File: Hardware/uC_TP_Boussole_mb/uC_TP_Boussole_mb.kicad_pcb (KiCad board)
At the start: 2 copper layers, 90 x 90 mm, 53 parts, among them J201 Conn_01x04, J301 Conn_01x05, J302 Conn_01x06, J401 Conn_01x02, J701 Conn_01x09, J801 Conn_01x04, SW301 SW_Push, SW302 SW_Push, SW303 SW_Push_DPDT, U201 TMC2225-SA-T, U301 STM32C011J4Mx, U402 AMS1117-3.3, U501 NUCLEO_L476RG

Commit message: update ppcb
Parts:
- added C601: 100n, Capacitor_SMD:C_0402_1005Metric, F.Cu at (70.4, 93.3)
- added U601: ~, Package_TO_SOT_SMD:SOT-363_SC-70-6, F.Cu at (71.0, 90.3)
- R601: value R_Small -> 30m
- moved C901 200.5 mm to (35.0, 89.1)
- moved C902 200.5 mm to (35.0, 91.1)
- moved C903 200.5 mm to (35.0, 93.0)
- moved C904 200.5 mm to (35.0, 95.0)
- moved R901 200.5 mm to (32.1, 89.1)
- moved R902 200.5 mm to (32.1, 91.1)
- moved R903 200.5 mm to (32.1, 93.1)
- moved R904 200.5 mm to (32.1, 95.1)
- moved R905 200.5 mm to (32.1, 97.1)
- moved R906 200.5 mm to (32.1, 99.0)
- moved J701 199.3 mm to (34.5, 112.0), turned to -90 degrees
- moved C801 197.9 mm to (32.5, 65.0)
- moved J801 197.9 mm to (28.8, 66.3)
- moved C701 188.6 mm to (43.5, 123.0)
- moved D401 188.2 mm to (76.8, 66.8)
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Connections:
- C402 pad 1: /Current_NCS199A3RSQT2G/Supply -> +3.3V
- C903 pad 1: /Rotary_Encodeur/ENC_BTN -> /NUCLEO_L476RG/ENC_BTN
- R403 pad 1: /Current_NCS199A3RSQT2G/Supply -> +3.3V
- R601 pad 1: /Current_NCS199A3RSQT2G/Supply -> +5V
- R601 pad 2: +3.3V -> /Current_NCS199A3RSQT2G/Load
- R906 pad 2: /Rotary_Encodeur/ENC_BTN -> /NUCLEO_L476RG/ENC_BTN
- U201 pad 20: /TMC2225_Driver/DIR -> /NUCLEO_L476RG/STEPPER_DIR
- U201 pad 21: /TMC2225_Driver/ENN -> /NUCLEO_L476RG/STEPPER_ENN
- U201 pad 25: /TMC2225_Driver/MS1 -> /NUCLEO_L476RG/STEPPER_MS1
- U201 pad 26: /TMC2225_Driver/MS2 -> /NUCLEO_L476RG/STEPPER_MS2
- U402 pad 2: /Current_NCS199A3RSQT2G/Supply -> +3.3V
- U501 pad 105: +3.3V -> unconnected-(U501A-VDD-Pad105)
- U501 pad 106: +5V -> /Current_NCS199A3RSQT2G/Load
- U501 pad 117: unconnected-(U501B-PA15-Pad117) -> /NUCLEO_L476RG/ENC_BTN
- U501 pad 132: unconnected-(U501B-PA4-Pad132) -> /Current_NCS199A3RSQT2G/Imes
- U501 pad 134: unconnected-(U501B-PB0-Pad134) -> /Magnetometre_BMM150_SEN0419/INT
- U501 pad 136: unconnected-(U501B-PC1-Pad136) -> /Magnetometre_BMM150_SEN0419/STATUS
- U501 pad 138: unconnected-(U501B-PC0-Pad138) -> /Magnetometre_BMM150_SEN0419/SPI_CS
- U501 pad 207: +3.3VA -> unconnected-(U501A-AVDD-Pad207)
- U501 pad 213: unconnected-(U501B-PA6-Pad213) -> /NUCLEO_L476RG/STEPPER_DIR
- U501 pad 214: unconnected-(U501B-PA11-Pad214) -> /NUCLEO_L476RG/STEPPER_MS1
- U501 pad 215: unconnected-(U501B-PA7-Pad215) -> /NUCLEO_L476RG/STEPPER_ENN
- U501 pad 216: unconnected-(U501B-PB12-Pad216) -> /NUCLEO_L476RG/STEPPER_MS2
- U501 pad 234: unconnected-(U501B-PC4-Pad234) -> /GPS_TEL0094_STM32C011J4M6/GPS_PPS
- U501 pad 235: unconnected-(U501B-PA2-Pad235) -> /GPS_TEL0094_STM32C011J4M6/GPS_EN

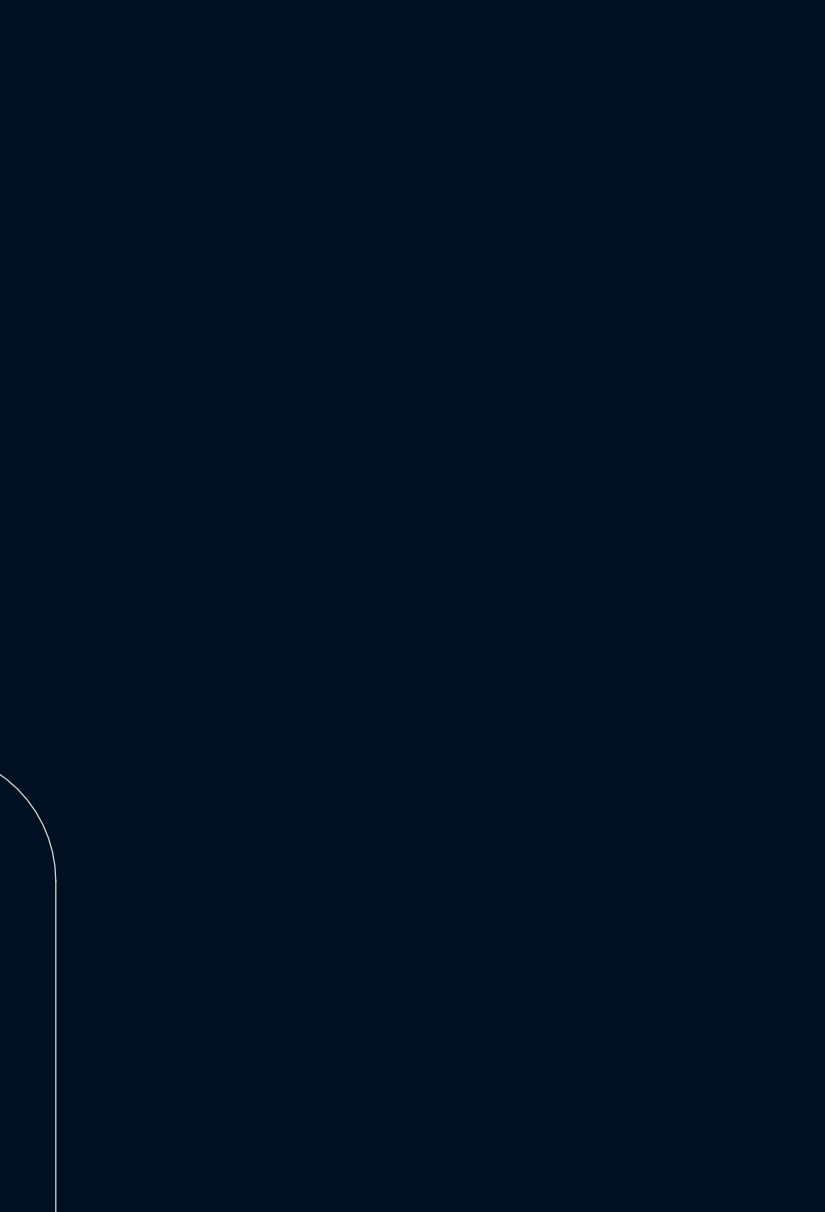
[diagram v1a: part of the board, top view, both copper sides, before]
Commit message: update schematic
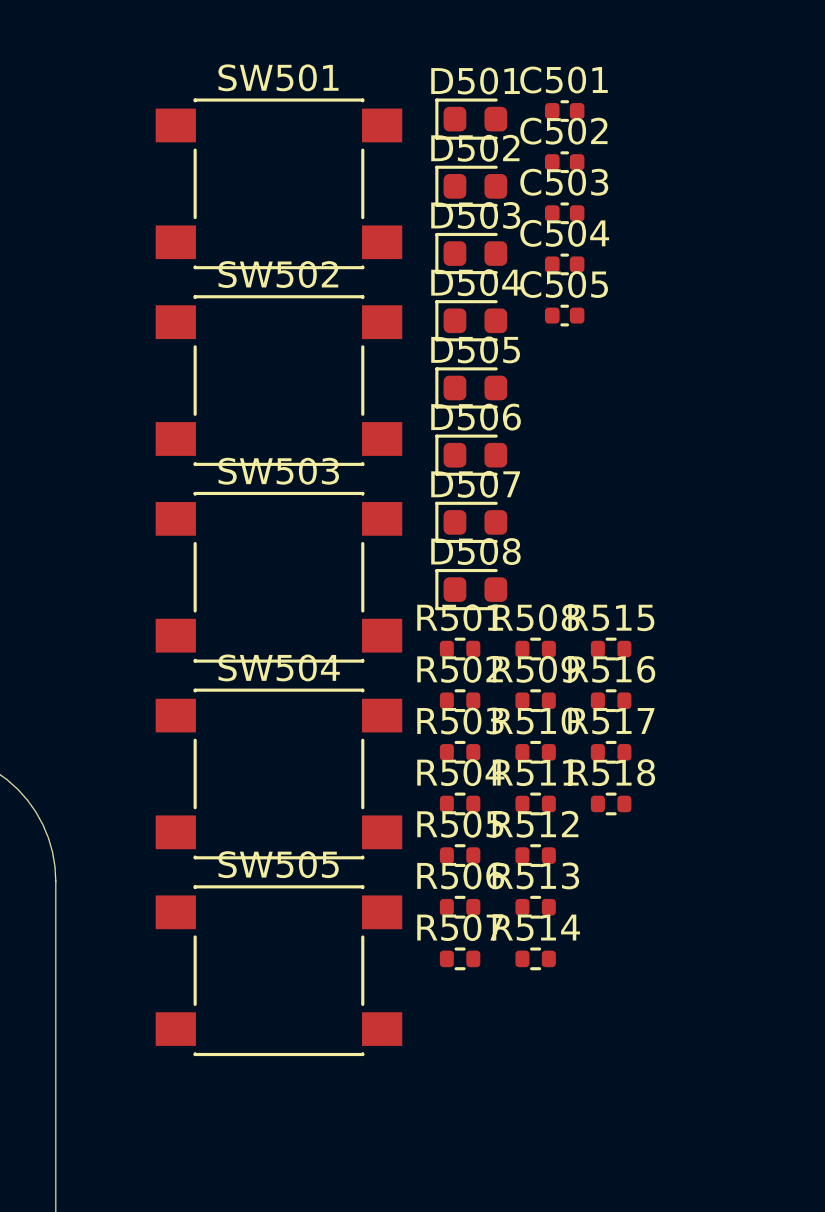
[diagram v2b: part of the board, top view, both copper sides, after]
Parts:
- added C501: 10n, Capacitor_SMD:C_0402_1005Metric, F.Cu at (159.6, 25.3)
- added C502: 10n, Capacitor_SMD:C_0402_1005Metric, F.Cu at (159.6, 27.3)
- added C503: 10n, Capacitor_SMD:C_0402_1005Metric, F.Cu at (159.6, 29.3)
- added C504: 10n, Capacitor_SMD:C_0402_1005Metric, F.Cu at (159.6, 31.2)
- added C505: 10n, Capacitor_SMD:C_0402_1005Metric, F.Cu at (159.6, 33.2)
- added D501: AMBER_LED, LED_SMD:LED_0603_1608Metric, F.Cu at (156.2, 25.6)
- added D502: RED_LED, LED_SMD:LED_0603_1608Metric, F.Cu at (156.2, 28.2)
- added D503: YELLOW_LED, LED_SMD:LED_0603_1608Metric, F.Cu at (156.2, 30.8)
- added D504: GREEN_LED, LED_SMD:LED_0603_1608Metric, F.Cu at (156.2, 33.4)
- added D505: GREEN_LED, LED_SMD:LED_0603_1608Metric, F.Cu at (156.2, 36.0)
- added D506: GREEN_LED, LED_SMD:LED_0603_1608Metric, F.Cu at (156.2, 38.6)
- added D507: GREEN_LED, LED_SMD:LED_0603_1608Metric, F.Cu at (156.2, 41.2)
- added D508: GREEN_LED, LED_SMD:LED_0603_1608Metric, F.Cu at (156.2, 43.8)
- added R501: 800, Resistor_SMD:R_0402_1005Metric, F.Cu at (155.6, 46.1)
- added R502: 850, Resistor_SMD:R_0402_1005Metric, F.Cu at (155.6, 48.0)
- added R503: 800, Resistor_SMD:R_0402_1005Metric, F.Cu at (155.6, 50.0)
- added R504: 400, Resistor_SMD:R_0402_1005Metric, F.Cu at (155.6, 52.0)
- added R505: 400, Resistor_SMD:R_0402_1005Metric, F.Cu at (155.6, 54.0)
- added R506: 400, Resistor_SMD:R_0402_1005Metric, F.Cu at (155.6, 56.0)
- added R507: 400, Resistor_SMD:R_0402_1005Metric, F.Cu at (155.6, 58.0)
- added R508: 400, Resistor_SMD:R_0402_1005Metric, F.Cu at (158.5, 46.1)
- added R509: 10k, Resistor_SMD:R_0402_1005Metric, F.Cu at (158.5, 48.0)
- added R510: 10k, Resistor_SMD:R_0402_1005Metric, F.Cu at (158.5, 50.0)
- added R511: 10k, Resistor_SMD:R_0402_1005Metric, F.Cu at (158.5, 52.0)
- added R512: 10k, Resistor_SMD:R_0402_1005Metric, F.Cu at (158.5, 54.0)
- added R513: 10k, Resistor_SMD:R_0402_1005Metric, F.Cu at (158.5, 56.0)
- added R514: 10k, Resistor_SMD:R_0402_1005Metric, F.Cu at (158.5, 58.0)
- added R515: 10k, Resistor_SMD:R_0402_1005Metric, F.Cu at (161.4, 46.1)
- added R516: 10k, Resistor_SMD:R_0402_1005Metric, F.Cu at (161.4, 48.0)
- added R517: 10k, Resistor_SMD:R_0402_1005Metric, F.Cu at (161.4, 50.0)
- added R518: 10k, Resistor_SMD:R_0402_1005Metric, F.Cu at (161.4, 52.0)
- added SW501: SW_Push, Button_Switch_SMD:SW_Push_1P1T_NO_6x6mm_H9.5mm, F.Cu at (148.6, 28.1)
- added SW502: SW_Push, Button_Switch_SMD:SW_Push_1P1T_NO_6x6mm_H9.5mm, F.Cu at (148.6, 35.7)
- added SW503: SW_Push, Button_Switch_SMD:SW_Push_1P1T_NO_6x6mm_H9.5mm, F.Cu at (148.6, 43.3)
- added SW504: SW_Push, Button_Switch_SMD:SW_Push_1P1T_NO_6x6mm_H9.5mm, F.Cu at (148.6, 50.9)
- added SW505: SW_Push, Button_Switch_SMD:SW_Push_1P1T_NO_6x6mm_H9.5mm, F.Cu at (148.6, 58.5)
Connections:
- U501 pad 201: unconnected-(U501B-PC9-Pad201) -> /NUCLEO_L476RG/BTN_LEFT
- U501 pad 202: unconnected-(U501B-PC8-Pad202) -> /NUCLEO_L476RG/BTN_RIGHT
- U501 pad 204: unconnected-(U501B-PC6-Pad204) -> /NUCLEO_L476RG/BTN_CENTER
- U501 pad 206: unconnected-(U501B-PC5-Pad206) -> /NUCLEO_L476RG/BTN_TOP
- U501 pad 211: /NUCLEO_L476RG/TIM3_CH1_STEPPER_PWM -> unconnected-(U501B-PA5-Pad211)
- U501 pad 212: unconnected-(U501B-PA12-Pad212) -> /NUCLEO_L476RG/STEPPER_ENN
- U501 pad 213: /NUCLEO_L476RG/STEPPER_DIR -> /NUCLEO_L476RG/TIM3_CH1_STEPPER_PWM
- U501 pad 215: /NUCLEO_L476RG/STEPPER_ENN -> /NUCLEO_L476RG/STEPPER_DIR
- U501 pad 218: unconnected-(U501B-PB11-Pad218) -> /NUCLEO_L476RG/BTN_BOT
- U501 pad 219: unconnected-(U501B-PC7-Pad219) -> /NUCLEO_L476RG/LED_0
- U501 pad 222: unconnected-(U501B-PB2-Pad222) -> /NUCLEO_L476RG/LED_1
- U501 pad 223: unconnected-(U501B-PA8-Pad223) -> /NUCLEO_L476RG/LED_2
- U501 pad 224: unconnected-(U501B-PB1-Pad224) -> /NUCLEO_L476RG/LED_3
- U501 pad 226: unconnected-(U501B-PB15-Pad226) -> /NUCLEO_L476RG/LED_4
- U501 pad 227: unconnected-(U501B-PB4-Pad227) -> /NUCLEO_L476RG/LED_5
- U501 pad 228: unconnected-(U501B-PB14-Pad228) -> /NUCLEO_L476RG/LED_6
- U501 pad 229: unconnected-(U501B-PB5-Pad229) -> /NUCLEO_L476RG/LED_7
- U501 pad 230: unconnected-(U501B-PB13-Pad230) -> /GPS_TEL0094_STM32C011J4M6/GPS_EN
- U501 pad 235: /GPS_TEL0094_STM32C011J4M6/GPS_EN -> unconnected-(U501B-PA2-Pad235)

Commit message: ddd
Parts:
- added J501: Conn_01x06, Connector_PinHeader_2.54mm:PinHeader_1x06_P2.54mm_Vertical, F.Cu at (24.6, 24.9)
- added J502: Conn_01x06, Connector_PinHeader_2.54mm:PinHeader_1x06_P2.54mm_Vertical, F.Cu at (29.2, 24.9)
- added J503: Conn_01x06, Connector_PinHeader_2.54mm:PinHeader_1x06_P2.54mm_Vertical, F.Cu at (33.9, 24.9)
- added R801: 1k, Resistor_SMD:R_0402_1005Metric, F.Cu at (-20.0, 81.5)
- added R802: 1k, Resistor_SMD:R_0402_1005Metric, F.Cu at (-20.0, 83.5)
- added SW901: RotaryEncoder_Switch, libs:482016514001_Mechanical_Incremental_Encoder_Switch, F.Cu at (-8.12, 3.40)
- added U401: 173010542, libs:173010xxx, F.Cu at (68.5, 10.5)
- R202: value 680 -> 680m
- U601: value ~ -> NCS199A3RSQT2G
- moved R601 98.4 mm to (-18.6, 45.3)
- moved C601 98.4 mm to (-18.7, 51.6)
- moved U601 98.4 mm to (-18.1, 48.6)
- moved C901 85.4 mm to (-7.52, 15.1)
- moved C902 85.4 mm to (-7.52, 17.0)
- moved C903 85.4 mm to (-7.52, 19.0)
- moved C904 85.4 mm to (-7.52, 21.0)
- moved R901 85.4 mm to (-10.4, 15.1)
- moved R902 85.4 mm to (-10.4, 17.1)
- moved R903 85.4 mm to (-10.4, 19.1)
- moved R904 85.4 mm to (-10.4, 21.0)
- moved R905 85.4 mm to (-10.4, 23.0)
- moved R906 85.4 mm to (-10.4, 25.0)
- moved C701 66.2 mm to (-20.5, 140.0)
- moved J701 66.2 mm to (-29.6, 129.0)
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- renumbered C504 to C502, C502 to C503, C505 to C504, C503 to C505, D502 to D501, D501 to D502, R515 to R511, R511 to R512, R517 to R513, R516 to R514, R512 to R515, R518 to R516, R513 to R517, R514 to R518, SW504 to SW502, SW502 to SW503, SW505 to SW504, SW503 to SW505
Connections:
- U501 pad 101: unconnected-(U501B-PC10-Pad101) -> /NUCLEO_L476RG/PC10
- U501 pad 102: unconnected-(U501B-PC11-Pad102) -> /NUCLEO_L476RG/PC11
- U501 pad 103: unconnected-(U501B-PC12-Pad103) -> /NUCLEO_L476RG/PC12
- U501 pad 104: unconnected-(U501B-PD2-Pad104) -> /NUCLEO_L476RG/PD2
- U501 pad 203: unconnected-(U501B-PB8-Pad203) -> /NUCLEO_L476RG/PB8
- U501 pad 205: unconnected-(U501B-PB9-Pad205) -> /NUCLEO_L476RG/PB9

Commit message: update schematic
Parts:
- removed the R301 at (210.7, 127.9)
- added C402: 22u, Capacitor_SMD:CP_Elec_5x5.4, F.Cu at (-79.0, 10.9)
- added C404: 100n, Capacitor_SMD:C_0402_1005Metric, F.Cu at (-73.1, 11.4)
- added D301: RED_LED, LED_SMD:LED_0603_1608Metric, F.Cu at (-65.3, 0.80)
- added D302: WE 82402375, libs:SC70-6L, F.Cu at (-65.7, 4.01)
- added D501: WE 82402374, libs:SC70-5L, F.Cu at (-81.8, 18.3)
- added D510: WE 82402374, libs:SC70-5L, F.Cu at (-78.5, 18.3)
- added D511: WE 82402375, libs:SC70-6L, F.Cu at (-75.2, 18.2)
- added D701: WE 82402374, libs:SC70-5L, F.Cu at (-65.7, 9.89)
- added D702: WE 82402374, libs:SC70-5L, F.Cu at (-62.4, 9.89)
- added D801: WE 82402374, libs:SC70-5L, F.Cu at (-70.0, 18.3)
- added D901: WE 82402374, libs:SC70-5L, F.Cu at (-64.7, 18.3)
- added R303: 800, Resistor_SMD:R_0402_1005Metric, F.Cu at (-62.6, 3.08)
- added R401: 1k, Resistor_SMD:R_0805_2012Metric, F.Cu at (-72.3, 8.95)
- added SW401: SW_SPDT, libs:472121020311, F.Cu at (-76.4, 3.52)
- renumbered C402 to C403, D501 to D502, D502 to D503, D503 to D504, D504 to D505, D505 to D506, D506 to D507, D507 to D508, D508 to D509, J502 to J501, J503 to J502, J501 to J503, R302 to R301, R303 to R302, R401 to R402, R402 to R403, R403 to R404
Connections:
- net Net-(R509-Pad2) renamed /NUCLEO_L476RG/BTN_L
- net Net-(R511-Pad2) renamed /NUCLEO_L476RG/BTN_T
- net Net-(R512-Pad2) renamed /NUCLEO_L476RG/BTN_C
- net Net-(R513-Pad2) renamed /NUCLEO_L476RG/BTN_B
- net Net-(R517-Pad2) renamed /NUCLEO_L476RG/BTN_R
- net Net-(R901-Pad2) renamed /Rotary_Encodeur/A
- net Net-(R902-Pad2) renamed /Rotary_Encodeur/B
- net Net-(R905-Pad2) renamed /Rotary_Encodeur/S
- J401 pad 2: +12V -> Net-(J401-Pin_2)
- SW303 pad 1: /GPS_TEL0094_STM32C011J4M6/STM32C0_RX -> unconnected-(SW303-A-Pad1)
- U301 pad 5: /GPS_TEL0094_STM32C011J4M6/STM32C0_RX -> /GPS_TEL0094_STM32C011J4M6/STM32C0_LED

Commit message: finalize pcb
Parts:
- added H101: MountingHole_Pad, MountingHole:MountingHole_3.2mm_M3_Pad, F.Cu at (55.0, 55.0)
- added H102: MountingHole_Pad, MountingHole:MountingHole_3.2mm_M3_Pad, F.Cu at (115.0, 55.0)
- added H103: MountingHole_Pad, MountingHole:MountingHole_3.2mm_M3_Pad, F.Cu at (175.0, 55.0)
- added H104: MountingHole_Pad, MountingHole:MountingHole_3.2mm_M3_Pad, F.Cu at (235.0, 55.0)
- added H105: MountingHole_Pad, MountingHole:MountingHole_3.2mm_M3_Pad, F.Cu at (235.0, 135.0)
- added H106: MountingHole_Pad, MountingHole:MountingHole_3.2mm_M3_Pad, F.Cu at (175.0, 135.0)
- added H107: MountingHole_Pad, MountingHole:MountingHole_3.2mm_M3_Pad, F.Cu at (115.0, 135.0)
- added H108: MountingHole_Pad, MountingHole:MountingHole_3.2mm_M3_Pad, F.Cu at (55.0, 135.0)
- added J402: Conn_02x02_Counter_Clockwise, Connector_PinHeader_2.54mm:PinHeader_2x02_P2.54mm_Vertical_SMD, F.Cu at (226.5, 54.9)
- added J504: Conn_02x10_Odd_Even, Connector_PinHeader_2.54mm:PinHeader_2x10_P2.54mm_Vertical_SMD, F.Cu at (80.0, 62.5)
- J201: moved to B.Cu
- J301: footprint Connector_PinHeader_2.54mm:PinHeader_1x05_P2.54mm_Vertical -> Connector_PinHeader_2.54mm:PinHeader_1x05_P2.54mm_Horizontal
- R204: footprint Resistor_SMD:R_0603_1608Metric_Pad0.98x0.95mm_HandSolder -> Resistor_SMD:R_0402_1005Metric
- moved D302 305.3 mm to (229.6, 81.6)
- moved D301 303.0 mm to (219.1, 105.5), turned to 90 degrees
- moved D511 299.6 mm to (210.0, 110.0), turned to 180 degrees
- moved R303 299.1 mm to (219.4, 103.0), turned to -90 degrees
- moved C402 291.2 mm to (208.9, 54.3), turned to -90 degrees
- moved R401 279.8 mm to (203.7, 54.7), turned to -90 degrees
- moved C404 279.7 mm to (203.7, 52.0), turned to -90 degrees
- moved SW401 277.0 mm to (196.0, 53.8)
- moved D701 224.4 mm to (152.1, 64.0), turned to 90 degrees
- moved D702 209.5 mm to (140.0, 64.0), turned to 90 degrees
- moved J701 197.0 mm to (155.0, 60.0), turned to 180 degrees
- moved C701 190.5 mm to (154.1, 63.8), turned to -90 degrees
- moved D901 189.2 mm to (96.2, 117.9), turned to 90 degrees
- moved D801 165.7 mm to (80.2, 88.4)
- moved D501 153.8 mm to (64.9, 64.3), turned to 90 degrees
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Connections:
- D302 pad 3: /GPS_TEL0094_STM32C011J4M6/GPS_EN -> /GPS_TEL0094_STM32C011J4M6/GPS_PPS
- D302 pad 4: /GPS_TEL0094_STM32C011J4M6/GPS_PPS -> /GPS_TEL0094_STM32C011J4M6/GPS_EN
- D501 pad 3: /NUCLEO_L476RG/PC12 -> /NUCLEO_L476RG/PC10
- D501 pad 5: /NUCLEO_L476RG/PC10 -> /NUCLEO_L476RG/PC12
- D510 pad 4: /NUCLEO_L476RG/PD2 -> /NUCLEO_L476RG/PB9
- D510 pad 5: /NUCLEO_L476RG/PB9 -> /NUCLEO_L476RG/PD2
- D511 pad 1: /NUCLEO_L476RG/BTN_B -> /NUCLEO_L476RG/BTN_R
- D511 pad 4: /NUCLEO_L476RG/BTN_R -> /NUCLEO_L476RG/BTN_L
- D511 pad 6: /NUCLEO_L476RG/BTN_L -> /NUCLEO_L476RG/BTN_B
- D701 pad 4: /Magnetometre_BMM150_SEN0419/STATUS -> /Magnetometre_BMM150_SEN0419/SPI_CLK
- D701 pad 5: /Magnetometre_BMM150_SEN0419/INT -> /Magnetometre_BMM150_SEN0419/SPI_MOSI
- D702 pad 1: /Magnetometre_BMM150_SEN0419/SPI_CLK -> /Magnetometre_BMM150_SEN0419/SPI_MISO
- D702 pad 3: /Magnetometre_BMM150_SEN0419/SPI_MOSI -> /Magnetometre_BMM150_SEN0419/SPI_CS
- D702 pad 4: /Magnetometre_BMM150_SEN0419/SPI_MISO -> /Magnetometre_BMM150_SEN0419/STATUS
- D702 pad 5: /Magnetometre_BMM150_SEN0419/SPI_CS -> /Magnetometre_BMM150_SEN0419/INT
- D801 pad 3: +3.3V -> /NUCLEO_L476RG/I2C1_SDA
- D801 pad 5: /NUCLEO_L476RG/I2C1_SDA -> +3.3V
- D901 pad 1: unconnected-(D901-I/O-Pad1) -> /Rotary_Encodeur/S
- D901 pad 3: /Rotary_Encodeur/S -> unconnected-(D901-I/O-Pad3)
- J201 pad 1: Net-(J201-Pin_1) -> /TMC2225_Driver/B2
- J201 pad 2: Net-(J201-Pin_2) -> /TMC2225_Driver/B1
- J201 pad 3: Net-(J201-Pin_3) -> /TMC2225_Driver/A1
- J201 pad 4: Net-(J201-Pin_4) -> /TMC2225_Driver/A2
- U201 pad 10: Net-(J201-Pin_4) -> /TMC2225_Driver/B2
- U201 pad 5: Net-(J201-Pin_2) -> /TMC2225_Driver/A2
- U201 pad 7: Net-(J201-Pin_1) -> /TMC2225_Driver/A1
- U201 pad 8: Net-(J201-Pin_3) -> /TMC2225_Driver/B1
- U501 pad 201: /NUCLEO_L476RG/BTN_LEFT -> /NUCLEO_L476RG/BTN_RIGHT
- U501 pad 202: /NUCLEO_L476RG/BTN_RIGHT -> /NUCLEO_L476RG/BTN_TOP
- U501 pad 204: /NUCLEO_L476RG/BTN_CENTER -> /NUCLEO_L476RG/BTN_LEFT
- U501 pad 206: /NUCLEO_L476RG/BTN_TOP -> /NUCLEO_L476RG/BTN_CENTER
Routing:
- net /GPS_TEL0094_STM32C011J4M6/GPS_PPS: track 0.00 -> 282.8 mm, vias 0 -> 7
- net /GPS_TEL0094_STM32C011J4M6/NUCLEO_RX: track 0.00 -> 207.0 mm, vias 0 -> 5
- net +5V: track 0.00 -> 175.1 mm, vias 0 -> 4
- net /GPS_TEL0094_STM32C011J4M6/NUCLEO_TX: track 0.00 -> 171.2 mm, vias 0 -> 5
- net /Magnetometre_BMM150_SEN0419/SPI_MOSI: track 0.00 -> 165.3 mm, vias 0 -> 3
- net /Magnetometre_BMM150_SEN0419/SPI_CLK: track 0.00 -> 161.3 mm, vias 0 -> 1
- net /Magnetometre_BMM150_SEN0419/SPI_MISO: track 0.00 -> 156.0 mm, vias 0 -> 3
- net /NUCLEO_L476RG/STEPPER_DIR: track 0.00 -> 154.1 mm, vias 0 -> 5
- net /NUCLEO_L476RG/STEPPER_MS2: track 0.00 -> 150.3 mm, vias 0 -> 4
- net /NUCLEO_L476RG/TIM3_CH1_STEPPER_PWM: track 0.00 -> 150.1 mm, vias 0 -> 5
- net /NUCLEO_L476RG/STEPPER_MS1: track 0.00 -> 147.0 mm, vias 0 -> 5
- net /NUCLEO_L476RG/STEPPER_ENN: track 0.00 -> 142.5 mm, vias 0 -> 5
- net /Magnetometre_BMM150_SEN0419/SPI_CS: track 0.00 -> 139.7 mm, vias 0 -> 3
- net /NUCLEO_L476RG/I2C1_SCL: track 0.00 -> 137.1 mm, vias 0 -> 7
- net /NUCLEO_L476RG/PB8: track 0.00 -> 133.8 mm, vias 0 -> 5
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- added copper zone on F.Cu, net +12V
- added copper zone on In1.Cu, net +12V
- added copper zone on In1.Cu, net +3.3V
- added copper zone on B.Cu, net GND
- added copper zone on F.Cu, net GND
- added copper zone on In2.Cu, net GND
- added copper zone on F.Cu, net Net-(C201-Pad2)
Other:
- board size 90 x 90 mm -> 190 x 90 mm
- copper layers 2 -> 4
- board text added: "12V"
- board text added: "3.3V"
- board text added: "5V"
- board text added: "DIR"
- board text added: "ENN"
- board text added: "Enc_A"
- board text added: "Enc_B"
- board text added: "Enc_Btn"
- board text added: "GND"
- board text added: "GPS_PPS"
- board text added: "GPS_RX"
- board text added: "GPS_TX"
- board text added: "I2C_SCL"
- board text added: "I2C_SDA"
- board text added: "Imes"
- board text added: "MS1"
- board text added: "MS2"
- board text added: "OFF"
- board text added: "ON"
- board text added: "PB8"
- board text added: "PB9"
- board text added: "PC10"
- board text added: "PC11"
- board text added: "PC12"
- board text added: "PD2"
- board text added: "SPI_CLK"
- board text added: "SPI_CS"
- board text added: "SPI_MISO"
- board text added: "SPI_MOSI"
- board text added: "STEP"
